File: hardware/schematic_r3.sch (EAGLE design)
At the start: 87 parts, among them Q1 SI2333DDS-T1-GE3CT-ND, U1 STM32L052K8, U2 BME280, U3 ADXL345, U4 HX1, U5 TPS62160, U6 TPS62160, U7 COPERNICUSSMD, U8 LMP7702, Y1 32.768kHz

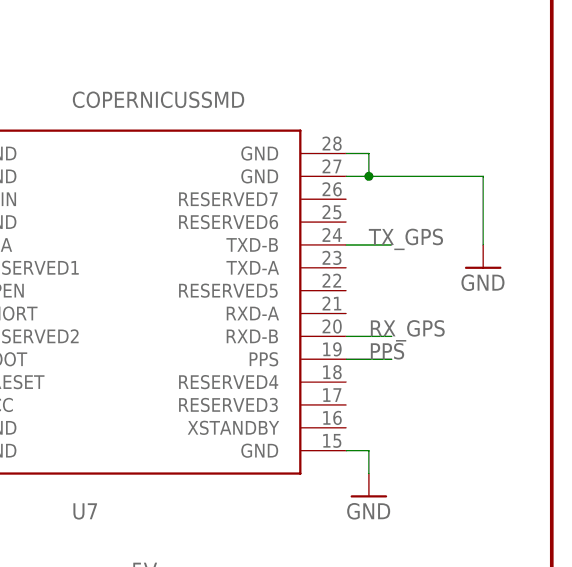
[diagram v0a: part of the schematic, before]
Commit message: Update r3 schematics and board to fix minor issues
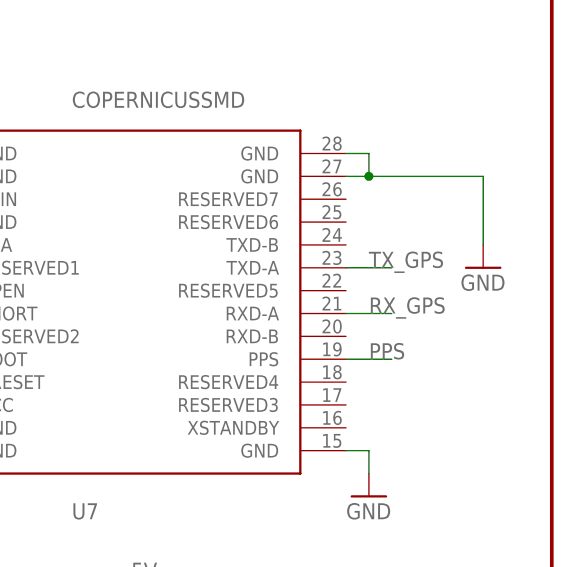
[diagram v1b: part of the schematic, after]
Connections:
- net RX_GPS: now also U7.RXD-A; no longer U7.RXD-B
- net TX_GPS: now also U7.TXD-A; no longer U7.TXD-B
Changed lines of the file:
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@@
 </segment>
 <segment>
-<pinref part="U7" gate="G$2" pin="TXD-B"/>
-<wire x1="487.68" y1="152.4" x2="482.6" y2="152.4" width="0.1524" layer="91"/>
-<label x="485.14" y="152.4" size="1.778" layer="95"/>
+<pinref part="U7" gate="G$2" pin="TXD-A"/>
+<wire x1="487.68" y1="149.86" x2="482.6" y2="149.86" width="0.1524" layer="91"/>
+<label x="485.14" y="149.86" size="1.778" layer="95"/>
 </segment>
 </net>
@@
 </segment>
 <segment>
-<pinref part="U7" gate="G$2" pin="RXD-B"/>
-<wire x1="487.68" y1="142.24" x2="482.6" y2="142.24" width="0.1524" layer="91"/>
-<label x="485.14" y="142.24" size="1.778" layer="95"/>
+<pinref part="U7" gate="G$2" pin="RXD-A"/>
+<wire x1="487.68" y1="144.78" x2="482.6" y2="144.78" width="0.1524" layer="91"/>
+<label x="485.14" y="144.78" size="1.778" layer="95"/>
 </segment>
 </net>
